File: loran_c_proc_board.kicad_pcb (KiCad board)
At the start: 2 copper layers, 170 x 100 mm, 252 parts, among them IC501 PC817, IC502 PC817, J201 RJ45, P101 Power, P102 Cortex SWD, P103 Clock board, P301 UART1 3V3, P302 DB9 Ribbon 2, P303 DB9 Ribbon 1, P401 SPI Bus A, P402 SPI Bus B, P501 RELAY A, P502 RELAY B, P503 RELAY C, P504 RELAY D, P601 DAC VCO, P602 DAC AGC, P603 QUAD In, P604 LORAN In, Q401 BC847, Q402 BC847, Q403 BC847, Q501 BC847, Q601 BD135, Q602 BD136, U101 LD1117S33, U102 74AC14, U201 LAN8720, U301 ST3232, U302 ST3232, U303 ST3232, U401 74AC14, U402 74AC14, U601 TL072, U602 LD1117S33, U701 STM32F407VG, X201 25MHz, X701 32.768KHz

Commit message: Update: PCB routing still in process...
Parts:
- removed C112, C113, C114: 100n, w_smd_capacitors:c_0805
- removed C503: 2.2u 6.3V Ta, w_smd_capacitors:c_tant_B
- removed Q401, Q402, Q403: BC847, SMD_Packages:SOT23
- removed R719: 33, w_smd_resistors:r_0805
- added C502: 100n, w_smd_capacitors:c_1206, B.Cu at (189.9, 122.0)
- added Q502: BC847, SMD_Packages:SOT23, F.Cu at (155.8, 120.5)
- added Q503: BC847, SMD_Packages:SOT23, F.Cu at (184.1, 116.5)
- added Q504: BC847, SMD_Packages:SOT23, F.Cu at (184.1, 111.2)
- added R108: 33, w_smd_resistors:r_1206, F.Cu at (81.9, 63.4)
- BT101: footprint w_battery_holders:keystone_103 -> battery-hold:bh840
- C102, C103, C501, D101, R105, R107, R701, R702: moved to B.Cu
- C110: footprint w_smd_capacitors:c_0805 -> w_smd_capacitors:c_1206; moved to B.Cu
- C601, C602, C609, C610, C611, C612, C707: moved to F.Cu
- C702, C703: footprint w_smd_capacitors:c_0603 -> w_smd_capacitors:c_0805
- C716: footprint w_smd_capacitors:c_0603 -> w_smd_capacitors:c_0805; moved to B.Cu
- FB102: footprint w_pth_resistors:RC07 -> w_pth_resistors:rc07_vert
- FB103: footprint w_smd_resistors:r_0805 -> w_pth_resistors:RC07
- R605, R606: footprint w_smd_resistors:r_1206 -> w_smd_resistors:r_0805; moved to F.Cu
- R703: footprint w_smd_resistors:r_1206 -> w_smd_resistors:r_0805
- R720: footprint w_smd_resistors:r_0805 -> w_smd_resistors:r_1206
- U101: footprint SMD_Packages:SOT223 -> Transistors_TO-220:TO-220_Neutral123_Vertical
- U601: footprint w_pth_ic:dil_8-300 -> w_smd_dil:so-8
- moved C612 169.0 mm to (108.7, 113.8), turned to 90 degrees
- moved R712 149.4 mm to (127.1, 74.5), turned to 270 degrees
- moved C611 144.9 mm to (113.3, 113.8), turned to 270 degrees
- moved R606 144.6 mm to (129.0, 119.8)
- moved P602 143.6 mm to (130.0, 124.5), turned to 180 degrees
- moved C601 143.6 mm to (120.3, 116.0), turned to 0 degrees
- moved C610 140.9 mm to (133.7, 113.5), turned to 0 degrees
- moved C609 140.5 mm to (120.3, 118.5), turned to 0 degrees
- moved R502 140.4 mm to (154.8, 129.7), turned to 180 degrees
- moved U601 140.3 mm to (127.0, 116.0)
- moved R501 140.3 mm to (151.0, 128.4), turned to 90 degrees
- moved P601 139.1 mm to (124.1, 124.5), turned to 180 degrees
- moved R605 138.3 mm to (125.0, 119.8)
- moved R509 135.6 mm to (159.9, 127.7), turned to 270 degrees
- moved C602 135.3 mm to (133.7, 116.0), turned to 0 degrees
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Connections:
- C106 pad 1: Net-(C106-Pad1) -> /CBL_VDD
- C107 pad 1: Net-(C106-Pad1) -> /CBL_VDD
- C109 pad 1: VDD -> /CBL_VDD
- C110 pad 1: /uC STM32F407/VBAT -> /CBL_VDD
- C111 pad 1: VDD -> /uC STM32F407/VBAT
- FB102 pad 1: VDD -> /CBL_VDD
- FB102 pad 2: Net-(C106-Pad1) -> VDD
- P503 pad 1: GND -> Net-(P503-Pad1)
- P503 pad 2: Net-(P503-Pad2) -> GND
- P504 pad 1: GND -> Net-(P504-Pad1)
- P504 pad 2: Net-(P504-Pad2) -> GND
- Q501 pad 3: /Relay optoisolation/RELAY4 -> Net-(Q501-Pad3)
- R104 pad 1: VDD -> /CB_OSC
- R104 pad 2: /CB_PPS_IN -> /CBL_VDD
- R105 pad 1: /CB_PPS_IN -> GND
- R105 pad 2: GND -> /CB_OSC
- R106 pad 1: VDD -> /CB_PPS_IN
- R106 pad 2: /CB_OSC -> /CBL_VDD
- R107 pad 1: /CB_OSC -> GND
- R107 pad 2: GND -> /CB_PPS_IN
- R501 pad 1: /Relay optoisolation/RELAY1 -> /uC STM32F407/RELAY1
- R501 pad 2: Net-(Q401-Pad1) -> Net-(Q501-Pad1)
- R502 pad 1: Net-(Q401-Pad1) -> Net-(Q501-Pad1)
- R503 pad 1: /Relay optoisolation/RELAY2 -> /uC STM32F407/RELAY2
- R505 pad 2: Net-(P503-Pad2) -> Net-(P503-Pad1)
- R508 pad 2: /Relay optoisolation/RELAY3 -> /uC STM32F407/RELAY3
- R509 pad 2: Net-(Q401-Pad3) -> Net-(Q501-Pad3)
- R511 pad 2: /Relay optoisolation/RELAY4 -> /uC STM32F407/RELAY4
- R512 pad 1: Net-(P503-Pad2) -> Net-(P503-Pad1)
- R513 pad 1: Net-(P504-Pad2) -> Net-(P504-Pad1)
- R514 pad 1: Net-(Q501-Pad1) -> Net-(Q504-Pad1)
- R514 pad 2: Net-(P504-Pad2) -> Net-(P504-Pad1)
- R515 pad 1: Net-(Q501-Pad1) -> Net-(Q504-Pad1)
- R711 pad 1: Net-(R706-Pad2) -> /Ethernet PHY/RMII_TX_EN
- R712 pad 1: Net-(R712-Pad1) -> /SPI interface/SPI_MOSI
- R718 pad 2: Net-(R712-Pad1) -> Net-(R718-Pad2)
- U102 pad 1: /uC STM32F407/PPS3 -> /CBL_VDD
- U102 pad 10: (no net) -> Net-(R103-Pad1)
- U102 pad 11: (no net) -> /uC STM32F407/PPS3
- U102 pad 12: Net-(R103-Pad1) -> Net-(R102-Pad2)
- U102 pad 13: /uC STM32F407/PPS3 -> /CB_OSC
- U102 pad 14: Net-(C106-Pad1) -> /CBL_VDD
- U102 pad 2: Net-(R103-Pad1) -> (no net)
- U102 pad 3: /CB_PPS_IN -> /uC STM32F407/PPS3
- U102 pad 4: /uC STM32F407/PPS_IN -> Net-(R103-Pad1)
- U102 pad 5: /CB_OSC -> GND
- U102 pad 6: Net-(R102-Pad2) -> (no net)
- U102 pad 8: (no net) -> Net-(R108-Pad2)
- U102 pad 9: (no net) -> /CB_PPS_IN
- U701 pad 41: (no net) -> /uC STM32F407/RELAY1
- U701 pad 42: (no net) -> /uC STM32F407/RELAY2
- U701 pad 43: (no net) -> /uC STM32F407/RELAY3
- U701 pad 44: (no net) -> /uC STM32F407/RELAY4
- U701 pad 47: Net-(R719-Pad2) -> /Ethernet PHY/RMII_NRST
- U701 pad 59: /Relay optoisolation/RELAY1 -> (no net)
- U701 pad 60: /Relay optoisolation/RELAY2 -> (no net)
- U701 pad 61: /Relay optoisolation/RELAY3 -> (no net)
- U701 pad 62: /Relay optoisolation/RELAY4 -> (no net)
- U701 pad 91: Net-(R712-Pad1) -> Net-(R718-Pad2)
- U701 pad 93: /uC STM32F407/PPS3 -> /uC STM32F407/PPS_IN
- U701 pad 95: /uC STM32F407/PPS_IN -> /uC STM32F407/PPS3
- X701 pad 1: /uC STM32F407/LSE_IN -> /uC STM32F407/LSE_OUT
- X701 pad 2: /uC STM32F407/LSE_OUT -> /uC STM32F407/LSE_IN
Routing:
- net VDD: track 189.0 -> 737.9 mm, vias 4 -> 5
- net +5VD: track 71.5 -> 202.4 mm, vias 0 -> 4
- net AGND: track 246.0 -> 151.9 mm, vias 8 -> 12
- net /CBL_VDD: track 0.00 -> 85.3 mm, vias 0 -> 3
- net /uC STM32F407/PPS3: track 11.3 -> 95.4 mm
- net /RS232 interface/UART1_RX: track 10.4 -> 75.7 mm, vias 1 -> 0
- net /RS232 interface/UART1_TX: track 10.5 -> 73.8 mm, vias 0 -> 2
- net /uC STM32F407/OSC_IN: track 35.5 -> 98.6 mm
- net /RS232 interface/UART1_CTS: track 4.07 -> 67.1 mm
- net /uC STM32F407/PPS_IN: track 6.11 -> 66.7 mm
- net /uC STM32F407/RELAY3: track 0.00 -> 55.0 mm, vias 0 -> 2
- net /RS232 interface/UART1_RTS: track 14.6 -> 66.2 mm
- net /uC STM32F407/RELAY4: track 0.00 -> 51.5 mm, vias 0 -> 2
- net /RS232 interface/UART2_RX: track 0.00 -> 49.0 mm
- net /RS232 interface/UART2_TX: track 0.00 -> 47.4 mm
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
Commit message: Update: PCB almost finished (3D views also up-to-date)
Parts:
- removed C616, C711: 10u 6.3V Ta, w_smd_capacitors:c_tant_B
- removed C623: 100n, w_smd_capacitors:c_1206
- removed D604: P6KE7V5 TVS, w_pth_diodes:diode_do15
- removed D605: SMLVT3V3, w_smd_diode:do214aa
- removed D702: BAS85, w_smd_diode:sod80c
- removed FB701: Bead, w_pth_resistors:RC07
- removed R609, R610, R616: Rt, w_smd_resistors:r_1210
- added P304: UART_SEL, Pin_Headers:Pin_Header_Straight_1x02, F.Cu at (178.1, 72.4)
- C607, C608: value 10u 16V -> 2.2u; footprint w_pth_capacitors:CP_5x11mm -> w_smd_capacitors:c_1206; moved to B.Cu
- C620, C621, D611, R612, R614, R615, R618: moved to B.Cu
- D603: value P6KE7V5 TVS -> SMLVT3V3; footprint w_pth_diodes:diode_do15 -> w_smd_diode:do214aa; moved to B.Cu
- FB103: footprint w_pth_resistors:RC07 -> SMD_Packages:SM1812E
- Q601, Q602: footprint Housings_SOT:SOT126_SOT32_Housing_Horizontal_RevA_22Oct2012 -> Housings_SOT:SOT126_SOT32_Housing_Vertical_BigPads
- R603, R604: footprint w_pth_resistors:RC07 -> w_pth_resistors:RC05
- moved D603 149.1 mm to (112.6, 120.0)
- moved C615 137.0 mm to (112.6, 122.1), turned to 0 degrees
- moved U602 128.8 mm to (112.6, 115.8), turned to 0 degrees
- moved C605 119.1 mm to (86.7, 97.4)
- moved Q601 117.6 mm to (78.9, 103.6), turned to 180 degrees
- moved C613 112.1 mm to (77.6, 112.2)
- moved C607 104.1 mm to (68.7, 106.7), turned to 90 degrees
- moved D601 102.5 mm to (68.7, 107.8)
- moved C617 102.4 mm to (121.8, 106.7), turned to 270 degrees
- moved R603 100.3 mm to (73.8, 99.6), turned to 180 degrees
- moved FB103 100.0 mm to (135.5, 105.4), turned to 0 degrees
- moved C604 89.1 mm to (96.5, 94.2)
- moved C603 88.7 mm to (96.5, 98.6)
- moved P604 85.8 mm to (100.3, 122.0), turned to 180 degrees
- moved R608 78.9 mm to (87.5, 119.3), turned to 180 degrees
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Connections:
- D603 pad 2: +7.5V -> +3.3VADC
- U102 pad 1: /CBL_VDD -> GND
- U303 pad 12: /RS232 interface/UART1_RX -> Net-(P304-Pad1)
- U303 pad 9: /RS232 interface/UART1_CTS -> Net-(P304-Pad2)
- U701 pad 15: /uC STM32F407/ADC3_IN -> /uC STM32F407/ADC1_IN
- U701 pad 17: /uC STM32F407/ADC1_IN -> /uC STM32F407/ADC2_IN
- U701 pad 18: /uC STM32F407/ADC2_IN -> /uC STM32F407/ADC3_IN
- X701 pad 1: /uC STM32F407/LSE_OUT -> /uC STM32F407/LSE_IN
- X701 pad 2: /uC STM32F407/LSE_IN -> /uC STM32F407/LSE_OUT
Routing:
- net AGND: track 151.9 -> 35.3 mm, vias 12 -> 13
- net -7.5V: track 58.8 -> 113.2 mm
- net /uC STM32F407/ADC3_IN: track 0.00 -> 46.4 mm
- net /uC STM32F407/ADC1_IN: track 15.2 -> 60.0 mm
- net +3.3VADC: track 73.1 -> 117.2 mm, vias 14 -> 16
- net /uC STM32F407/ADC2_IN: track 15.2 -> 52.8 mm
- net /RS232 interface/UART1_RX: track 75.7 -> 43.5 mm
- net /Analog part/+15V_AS: track 52.1 -> 20.7 mm
- net /Analog part/-15V_AS: track 55.8 -> 25.8 mm
- net Net-(P304-Pad1): track 0.00 -> 29.7 mm
- net /RS232 interface/UART1_CTS: track 67.1 -> 42.8 mm
- net Net-(P304-Pad2): track 0.00 -> 21.7 mm
- net +7.5V: track 65.6 -> 83.4 mm
- net /Analog part/+15V: track 0.00 -> 17.2 mm
- net Net-(R103-Pad1): track 24.8 -> 9.55 mm
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- removed copper zone on F.Cu, net /Analog part/+15V_AS
- removed copper zone on F.Cu, net /Analog part/-15V_AS
- removed copper zone on F.Cu, net VDD

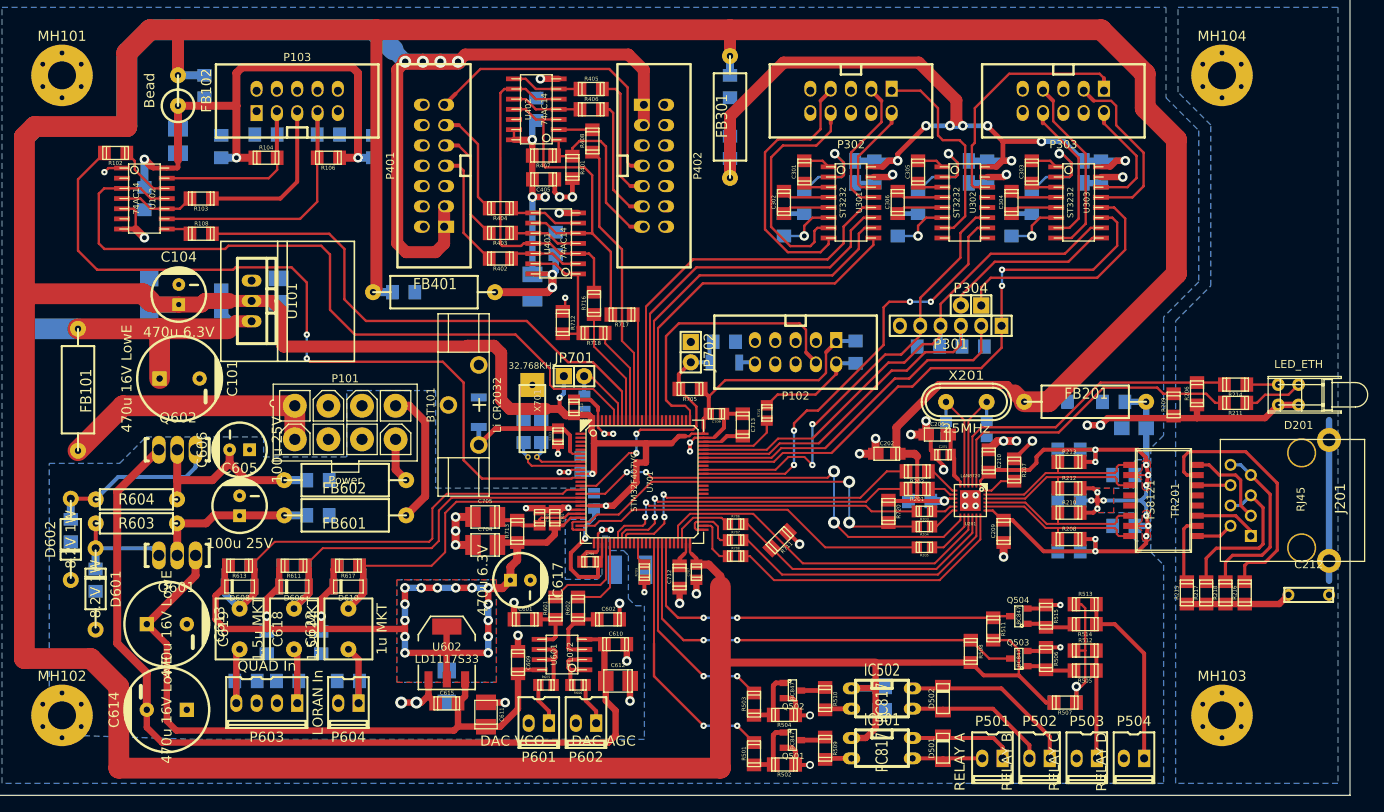
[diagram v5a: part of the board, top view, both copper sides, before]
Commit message: Update PCB: fix drill diameters (now only 8 required)
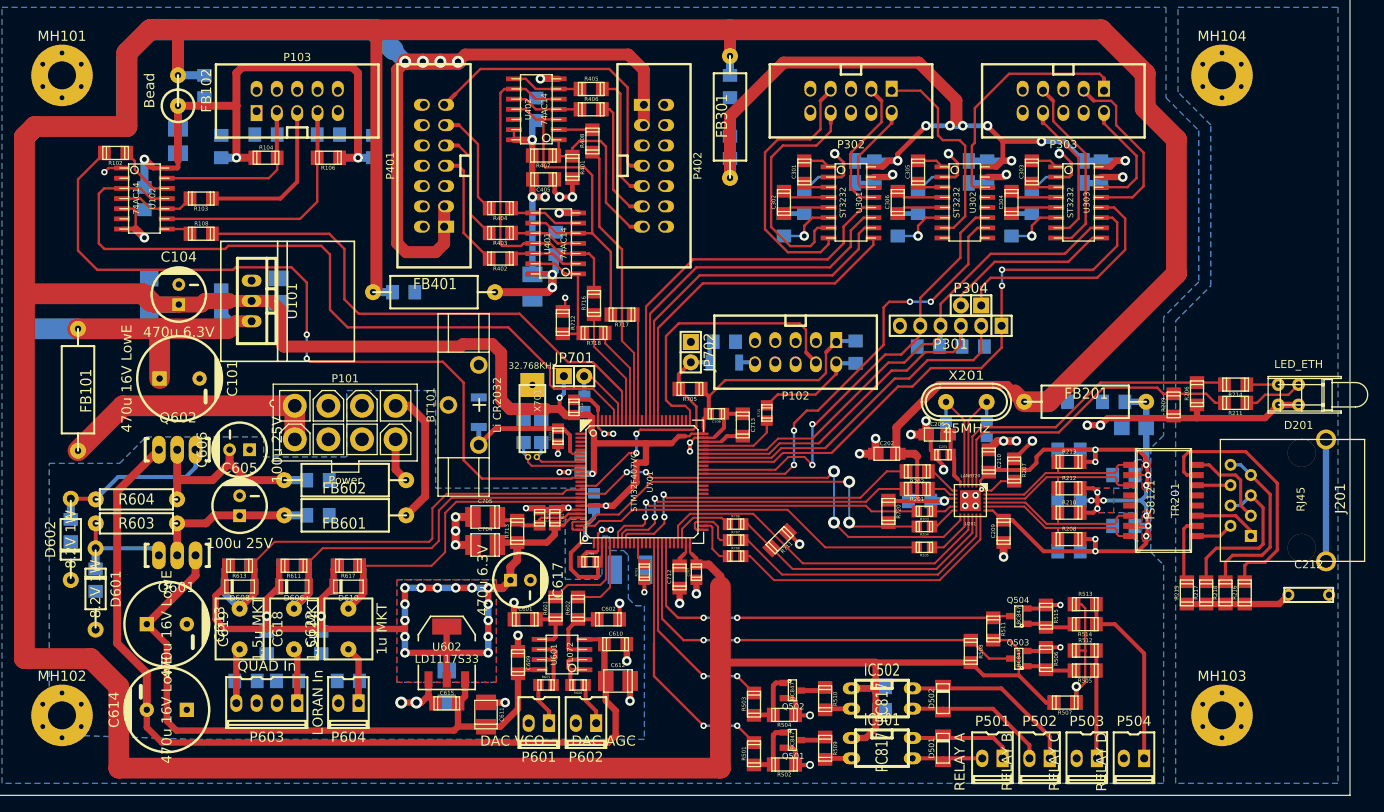
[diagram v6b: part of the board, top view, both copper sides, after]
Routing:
- net GNDPWR: track 20.1 -> 15.2 mm
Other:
- net class 3v3_power removed

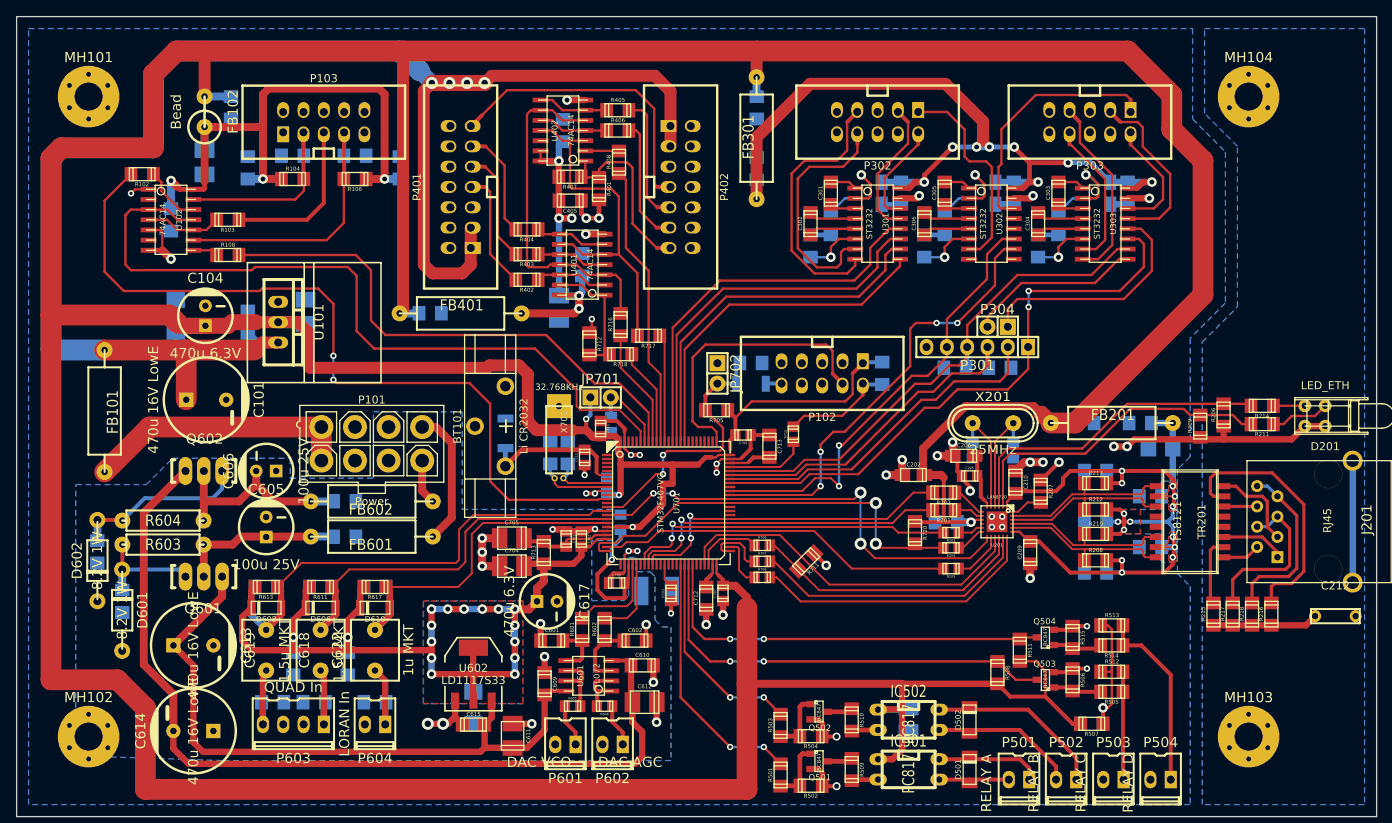
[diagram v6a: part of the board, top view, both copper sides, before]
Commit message: PCB Update: no more tracks underneath SMD 0805, added text
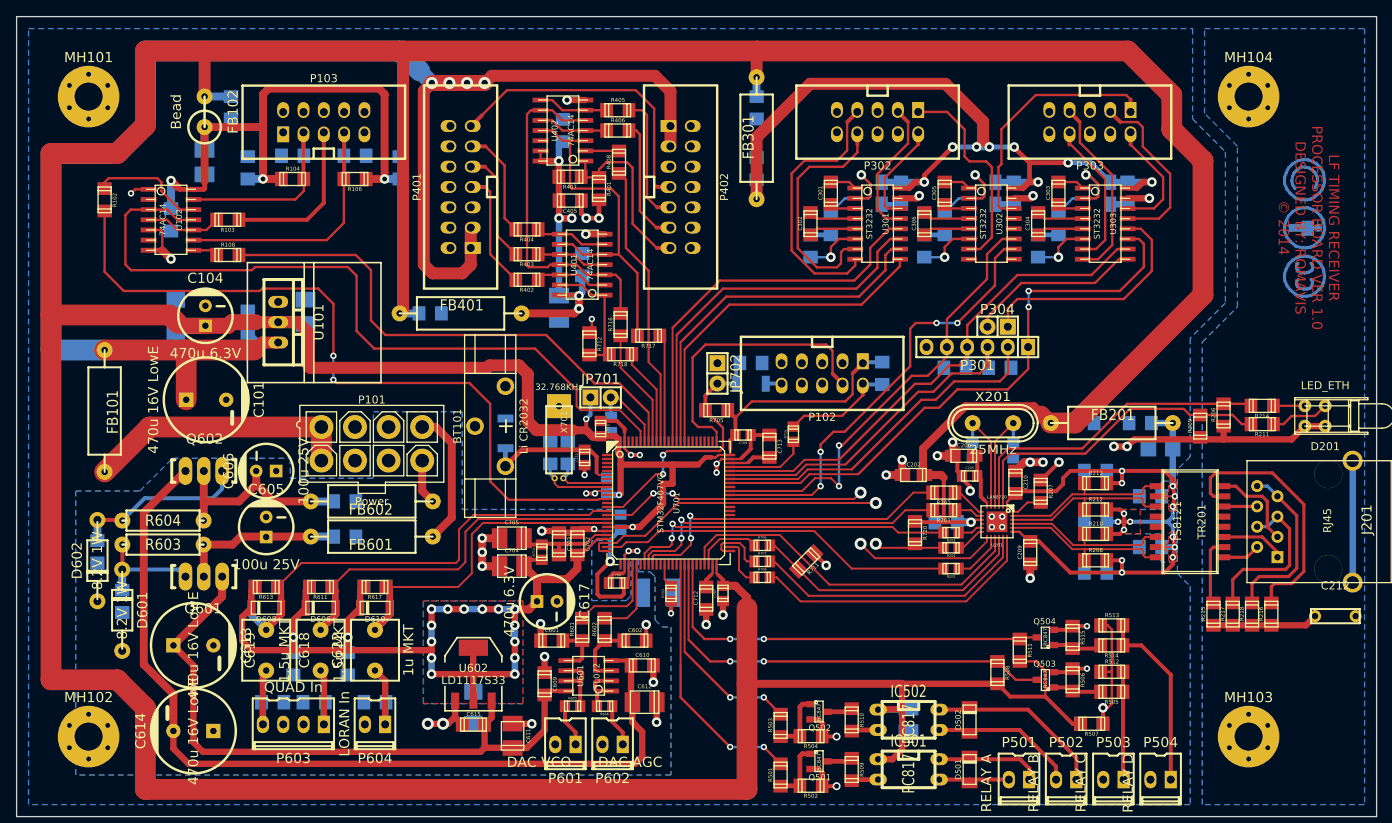
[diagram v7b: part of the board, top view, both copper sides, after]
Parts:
- added LIC1: CC, Footprint_Symbols:Symbol_CreativeCommons_CopperTop_Type2_Small, B.Cu at (216.4, 66.2)
- added LIC2: BY, Footprint_Symbols:Symbol_CC-Attribution_CopperTop_Small, B.Cu at (216.5, 60.0)
- added LIC3: SA, Footprint_Symbols:Symbol_CC-ShareAlike_CopperTop_Small, B.Cu at (216.5, 54.0)
- C702, C703: footprint w_smd_capacitors:c_0805 -> w_smd_capacitors:c_1206
- R713: footprint w_smd_resistors:r_1206 -> w_smd_resistors:r_0805
- moved R102 5.69 mm to (66.5, 56.5), turned to 270 degrees
- moved C703 1.08 mm to (123.3, 99.5)
- moved C702 0.78 mm to (125.6, 99.5)
- moved FB103 0.28 mm to (135.7, 105.6)
- moved R713 0.25 mm to (121.2, 100.5)
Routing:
- net Net-(R102-Pad2): track 7.47 -> 14.4 mm
- net /uC STM32F407/OSC_IN: track 99.7 -> 93.8 mm
- net +3.3VADC: track 117.2 -> 119.1 mm
- net AGND: track 35.3 -> 36.7 mm
- net Net-(C703-Pad1): track 11.9 -> 12.6 mm
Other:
- copper layers 2 -> 4
- board text added: "LF TIMING RECEIVER PROCESSOR BOARD VER 1.0 DESIGNED BY: ROMAVIS © 2014"
